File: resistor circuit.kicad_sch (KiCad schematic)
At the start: 10 parts

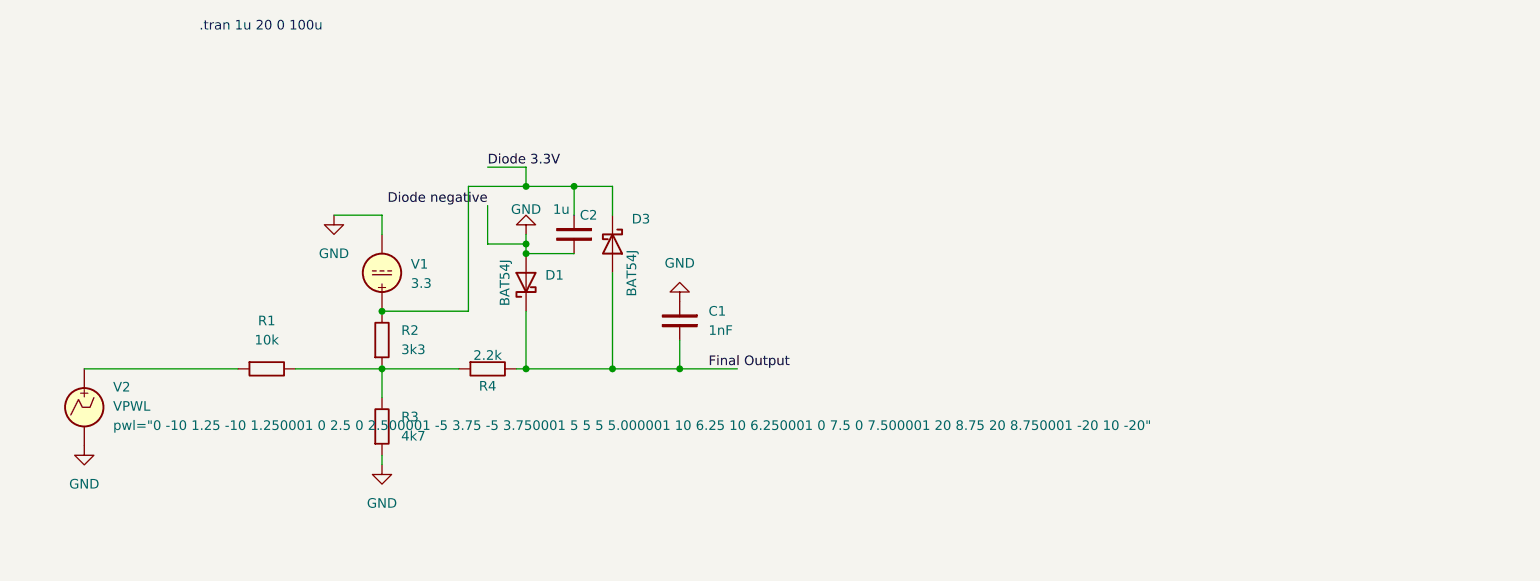
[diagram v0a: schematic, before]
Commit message: add 100 ohm resistor
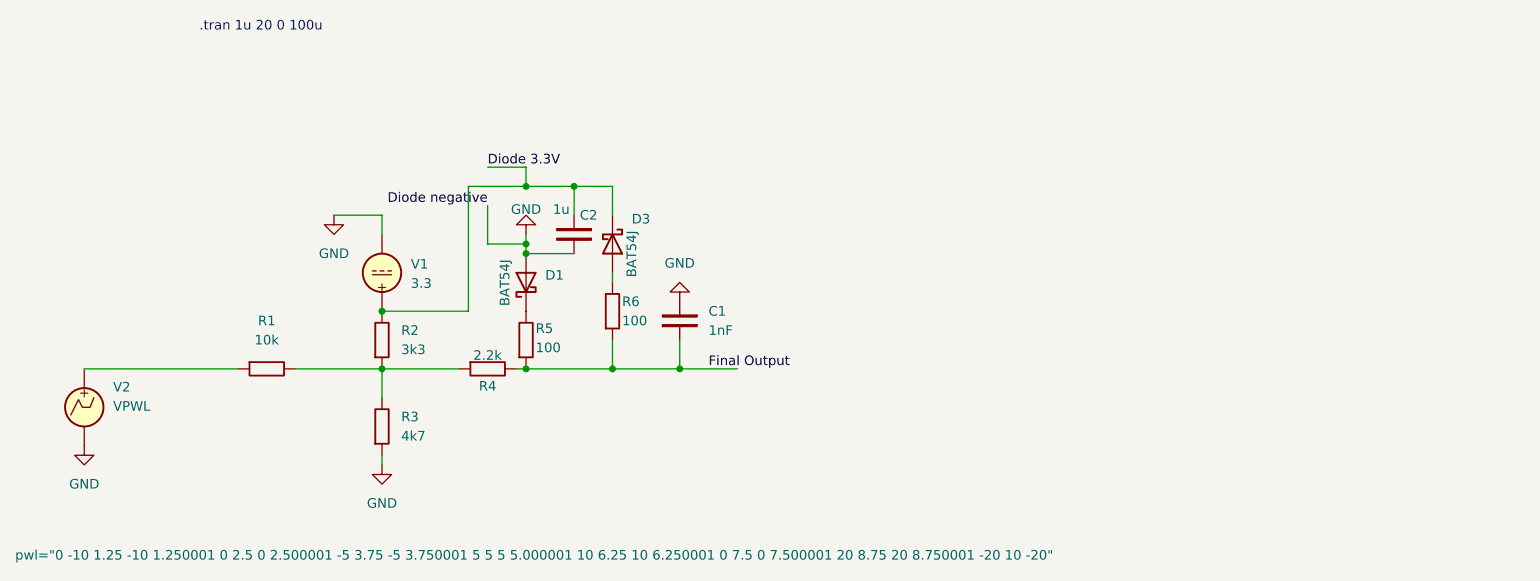
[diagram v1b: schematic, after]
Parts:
- added R5, R6: 100, Resistor_THT:R_Axial_DIN0207_L6.3mm_D2.5mm_P10.16mm_Horizontal, symbol PCM_SL_Resistors:Resistor
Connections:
- net Final Output: now also R5.1, R6.1; no longer D1.1 (K), D3.2 (A)
- new net: D3.2 (A), R6.2
- new net: D1.1 (K), R5.2
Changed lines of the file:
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@@
 	(wire
 		(pts
-			(xy 134.62 52.07) (xy 134.62 64.77)
+			(xy 134.62 52.07) (xy 134.62 53.34)
 		)
 		(stroke
@@
 	(wire
 		(pts
-			(xy 123.19 57.15) (xy 123.19 64.77)
-		)
-		(stroke
-			(width 0)
-			(type default)
-		)
-	)
-	(wire
-		(pts
 			(xy 104.14 44.45) (xy 104.14 46.99)
 		)
@@
 		(pts
 			(xy 104.14 76.2) (xy 104.14 77.47)
+		)
+		(stroke
+			(width 0)
+			(type default)
+		)
+	)
+	(wire
+		(pts
+			(xy 134.62 60.96) (xy 134.62 64.77)
 		)
 		(stroke
@@
 		)
 		(property "Value" "BAT54J"
-			(at 137.16 49.022 0)
+			(at 137.16 46.482 0)
 			(effects
 				(font
@@
 				(path "/509d3974-e6ed-414a-b815-782fed6f3dc0"
 					(reference "D3")
+					(unit 1)
+				)
+			)
+		)
+	)
+	(symbol
+		(lib_id "PCM_SL_Resistors:Resistor")
+		(at 134.62 57.15 90)
+		(unit 1)
+		(exclude_from_sim no)
+		(in_bom yes)
+		(on_board yes)
+		(dnp no)
+		(property "Reference" "R6"
+			(at 135.89 55.88 90)
+			(effects
+				(font
+					(size 1.27 1.27)
+				)
+				(justify right)
+			)
+		)
+		(property "Value" "100"
+			(at 135.89 58.42 90)
+			(effects
+				(font
+					(size 1.27 1.27)
+				)
+				(justify right)
+			)
+		)
+		(property "Footprint" "Resistor_THT:R_Axial_DIN0207_L6.3mm_D2.5mm_P10.16mm_Horizontal"
+			(at 138.938 56.261 0)
+			(effects
+				(font
+					(size 1.27 1.27)
+				)
+				(hide yes)
+			)
+		)
+		(property "Datasheet" ""
+			(at 134.62 56.642 0)
+			(effects
+				(font
+					(size 1.27 1.27)
+				)
+				(hide yes)
+			)
+		)
+		(property "Description" "1/4W Resistor"
+			(at 134.62 57.15 0)
+			(effects
+				(font
+					(size 1.27 1.27)
+				)
+				(hide yes)
+			)
+		)
+		(pin "1"
+		)
+		(pin "2"
+		)
+		(instances
+			(project "resistor circuit"
+				(path "/509d3974-e6ed-414a-b815-782fed6f3dc0"
+					(reference "R6")
 					(unit 1)
 				)
@@
 	)
 	(symbol
+		(lib_id "PCM_SL_Resistors:Resistor")
+		(at 123.19 60.96 90)
+		(unit 1)
+		(exclude_from_sim no)
+		(in_bom yes)
+		(on_board yes)
+		(dnp no)
+		(property "Reference" "R5"
+			(at 124.46 59.436 90)
+			(effects
+				(font
+					(size 1.27 1.27)
+				)
+				(justify right)
+			)
+		)
+		(property "Value" "100"
+			(at 124.46 61.976 90)
+			(effects
+				(font
+					(size 1.27 1.27)
+				)
+				(justify right)
+			)
+		)
+		(property "Footprint" "Resistor_THT:R_Axial_DIN0207_L6.3mm_D2.5mm_P10.16mm_Horizontal"
+			(at 127.508 60.071 0)
+			(effects
+				(font
+					(size 1.27 1.27)
+				)
+				(hide yes)
+			)
+		)
+		(property "Datasheet" ""
+			(at 123.19 60.452 0)
+			(effects
+				(font
+					(size 1.27 1.27)
+				)
+				(hide yes)
+			)
+		)
+		(property "Description" "1/4W Resistor"
+			(at 123.19 60.96 0)
+			(effects
+				(font
+					(size 1.27 1.27)
+				)
+				(hide yes)
+			)
+		)
+		(pin "1"
+		)
+		(pin "2"
+		)
+		(instances
+			(project "resistor circuit"
+				(path "/509d3974-e6ed-414a-b815-782fed6f3dc0"
+					(reference "R5")
+					(unit 1)
+				)
+			)
+		)
+	)
+	(symbol
 		(lib_id "Diode:BAT54J")
 		(at 123.19 53.34 90)
@@
 		(on_board yes)
 		(dnp no)
-		(fields_autoplaced yes)
 		(property "Reference" "V2"
 			(at 68.58 67.1801 0)
@@
 		)
 		(property "Sim.Params" "pwl=\"0 -10 1.25 -10 1.250001 0 2.5 0 2.500001 -5 3.75 -5 3.750001 5 5 5 5.000001 10 6.25 10 6.250001 0 7.5 0 7.500001 20 8.75 20 8.750001 -20 10 -20\""
-			(at 68.58 72.2601 0)
-			(effects
-				(font
+			(at 55.626 89.408 0)
+			(effects
+				(font
